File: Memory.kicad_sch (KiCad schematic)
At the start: 8 parts, among them U3 28C256, U4 74HC32, U5 62256, U6 74HC32, U7 74HC00, U8 62256, U9 74HC04

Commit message: Schematic cleanup
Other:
- moved on the sheet: JP1, U3, U4A, U4B, U5, U6A, U6B, U6C, U6D, U7A, U7B, U8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

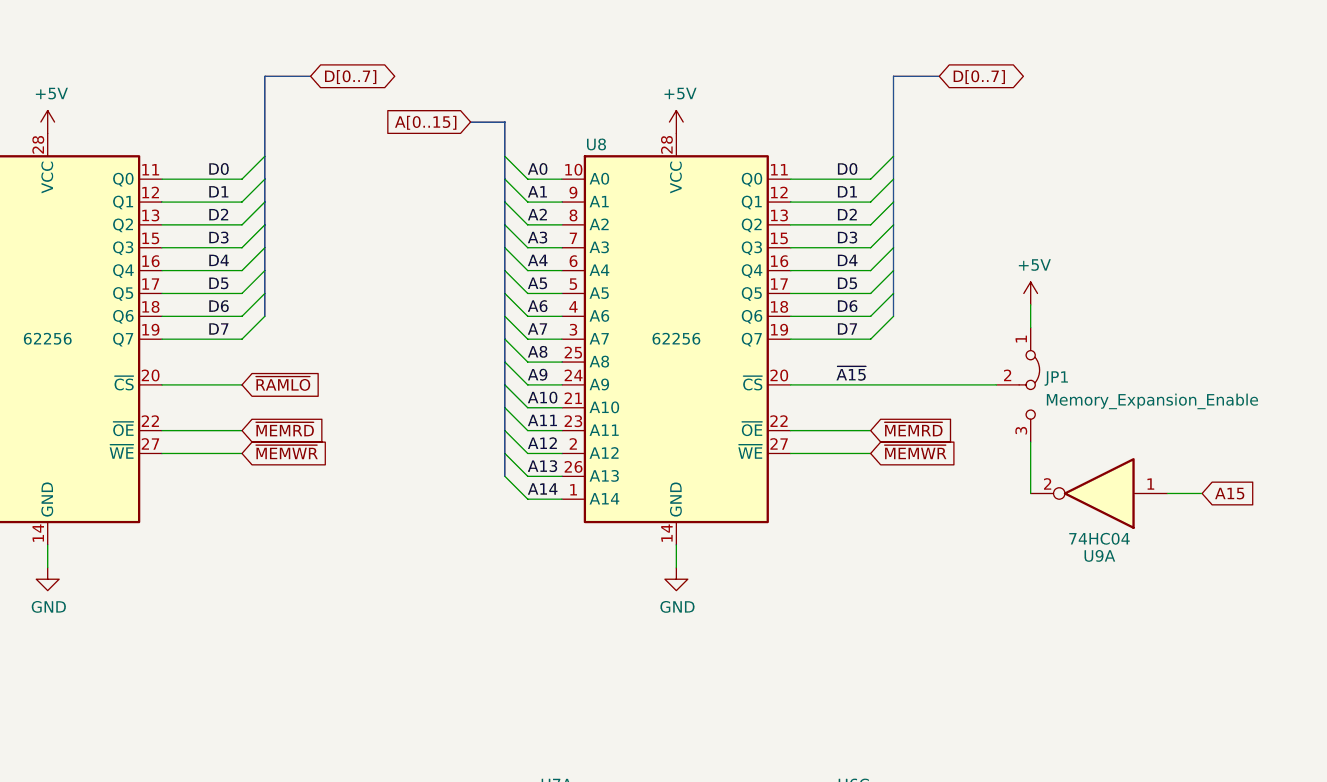
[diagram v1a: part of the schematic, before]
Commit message: Memory expansion moved to low memory
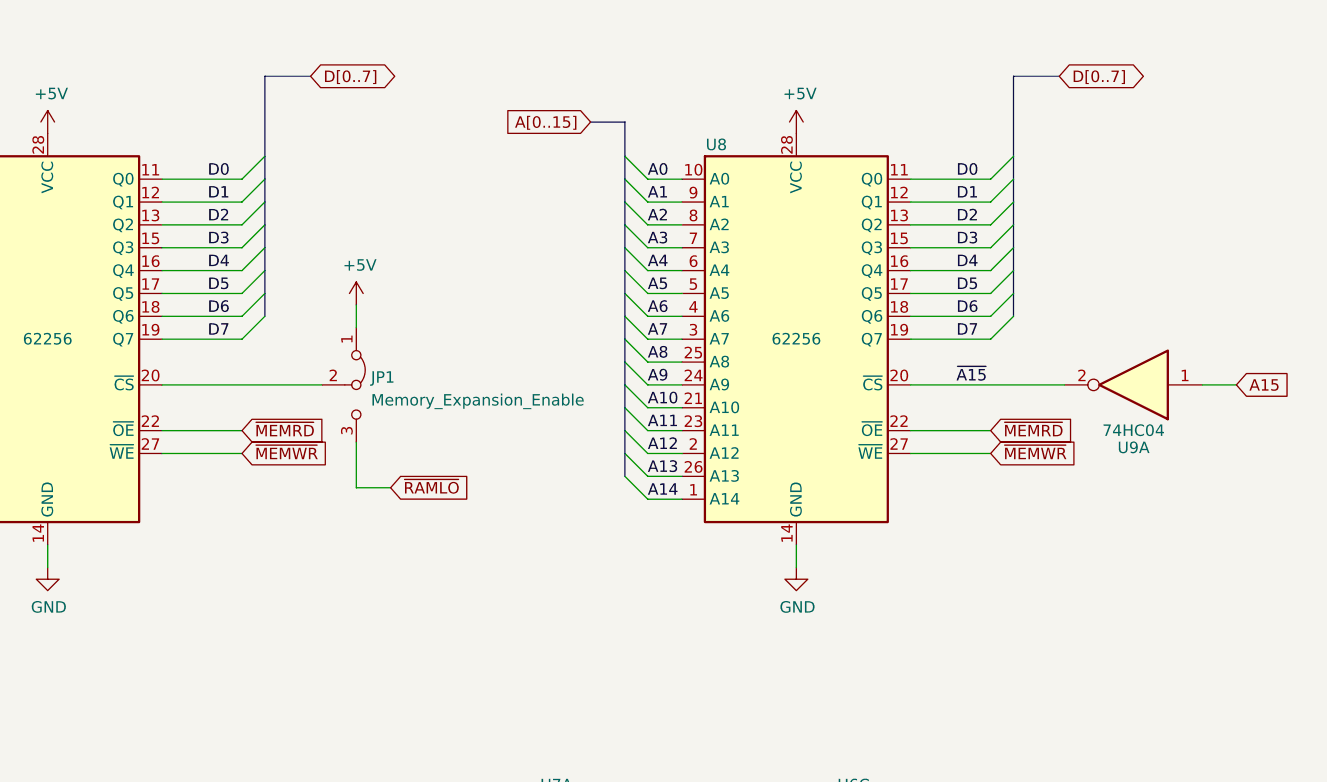
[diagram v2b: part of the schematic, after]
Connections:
- net ~{A15}: now also U9.2; no longer JP1.2 (C)
- net ~{RAMLO}: now also JP1.3 (B); no longer U5.20 (~{CS})
- new net: JP1.2 (C), U5.20 (~{CS})
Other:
- moved on the sheet: JP1, U8, U9A

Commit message: Misc Updates/Cleanup
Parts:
- U4, U6: value 74HC32 -> 74HCT32
- U7: value 74HC00 -> 74HCT00
- U9: value 74HC04 -> 74HCT04
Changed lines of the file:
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@@
       (effects (font (size 1.27 1.27)))
     )
-    (property "Value" "74HC04" (at 248.285 70.485 0)
+    (property "Value" "74HCT04" (at 248.285 70.485 0)
       (effects (font (size 1.27 1.27)))
     )
@@
       (effects (font (size 1.27 1.27)))
     )
-    (property "Value" "74HC00" (at 184.15 112.1664 0)
+    (property "Value" "74HCT00" (at 184.15 112.1664 0)
       (effects (font (size 1.27 1.27)))
     )
@@
       (effects (font (size 1.27 1.27)))
     )
-    (property "Value" "74HC00" (at 184.15 144.78 0)
+    (property "Value" "74HCT00" (at 184.15 144.78 0)
       (effects (font (size 1.27 1.27)))
     )
@@
       (effects (font (size 1.27 1.27)))
     )
-    (property "Value" "74HC32" (at 142.24 131.2164 0)
+    (property "Value" "74HCT32" (at 142.24 131.2164 0)
       (effects (font (size 1.27 1.27)))
     )
@@
       (effects (font (size 1.27 1.27)))
     )
-    (property "Value" "74HC32" (at 217.17 131.2164 0)
+    (property "Value" "74HCT32" (at 217.17 131.2164 0)
       (effects (font (size 1.27 1.27)))
     )
@@
       (effects (font (size 1.27 1.27)))
     )
-    (property "Value" "74HC32" (at 217.17 112.1664 0)
+    (property "Value" "74HCT32" (at 217.17 112.1664 0)
       (effects (font (size 1.27 1.27)))
     )
@@
       (effects (font (size 1.27 1.27)))
     )
-    (property "Value" "74HC32" (at 164.465 133.7564 0)
+    (property "Value" "74HCT32" (at 164.465 133.7564 0)
       (effects (font (size 1.27 1.27)))
     )
@@
       (effects (font (size 1.27 1.27)))
     )
-    (property "Value" "74HC32" (at 62.865 124.2314 0)
+    (property "Value" "74HCT32" (at 62.865 124.2314 0)
       (effects (font (size 1.27 1.27)))
     )
@@
       (effects (font (size 1.27 1.27)))
     )
-    (property "Value" "74HC04" (at 142.24 147.32 0)
+    (property "Value" "74HCT04" (at 142.24 147.32 0)
       (effects (font (size 1.27 1.27)))
     )
@@
       (effects (font (size 1.27 1.27)))
     )
-    (property "Value" "74HC32" (at 62.865 139.4714 0)
-      (effects (font (size 1.27 1.27)))
-    )
+    (property "Value" "74HCT32" (at 62.865 139.4714 0)
+      (effects (font (size 1.27 1.27)))
+    )

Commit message: Work-in-progress
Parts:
- U12: renamed from U6; footprint Package_DIP:DIP-14_W7.62mm_LongPads -> Package_DIP:DIP-14_W7.62mm
- U3, U5, U8: footprint Package_DIP:DIP-28_W15.24mm_LongPads -> Package_DIP:DIP-28_W15.24mm
- U4, U6, U7, U9: footprint Package_DIP:DIP-14_W7.62mm_LongPads -> Package_DIP:DIP-14_W7.62mm
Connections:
- net +5V: now also JP1.3 (B); no longer JP1.1 (A)
- net ~{A15}: now also JP1.2 (C); no longer U9.2
- net ~{RAMLO}: now also U5.20 (~{CS}); no longer JP1.3 (B)
- net ~{SLOT0}: now also U12.5; no longer U12.2
- net ~{WR}: now also U12.4; no longer U12.1
- net at U7.5: now also U12.8; no longer U12.6
- net at U9.4: now also U12.10; no longer U12.5
- new net: JP1.1 (A), U9.2
- new net: U12.6, U12.9
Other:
- moved on the sheet: JP1, U9A
